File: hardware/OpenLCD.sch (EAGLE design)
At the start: 39 parts, among them Q1 PNP-500mA, Q2 PNP-500mA, Q3 PNP-500mA, U1 ATMEGA328P_TQFP, U2 4BIT-RGB, U3 MIC5205-ADJ, Y2 8MHz

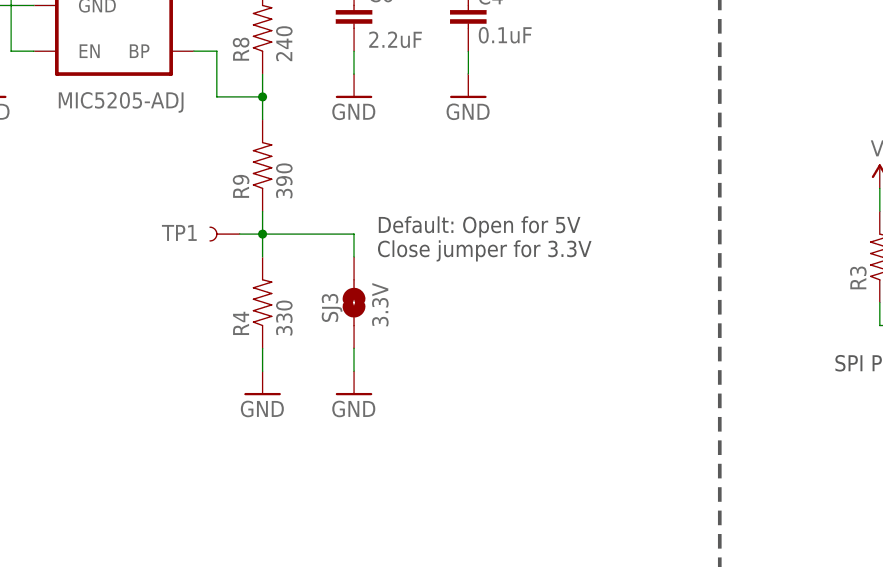
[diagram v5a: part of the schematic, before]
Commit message: Correcting silk
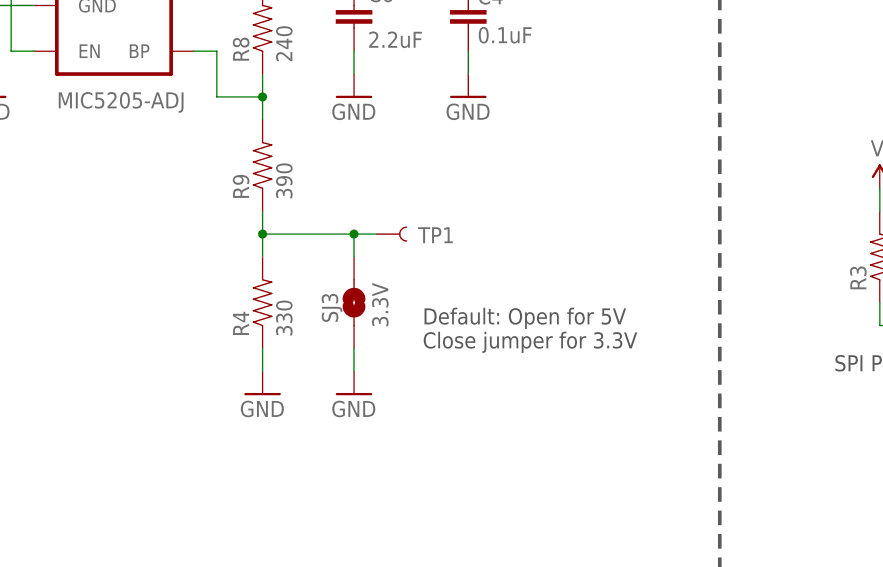
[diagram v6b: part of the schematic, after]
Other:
- moved on the sheet: TP1
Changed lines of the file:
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@@
 <grid distance="0.1" unitdist="inch" unit="inch" style="lines" multiple="1" display="no" altdistance="0.01" altunitdist="inch" altunit="inch"/>
 <layers>
-<layer number="1" name="Top" color="4" fill="1" visible="yes" active="no"/>
-<layer number="2" name="Route2" color="1" fill="3" visible="yes" active="no"/>
-<layer number="3" name="Route3" color="4" fill="3" visible="yes" active="no"/>
-<layer number="4" name="Route4" color="1" fill="4" visible="yes" active="no"/>
-<layer number="5" name="Route5" color="4" fill="4" visible="yes" active="no"/>
-<layer number="6" name="Route6" color="1" fill="8" visible="yes" active="no"/>
-<layer number="7" name="Route7" color="4" fill="8" visible="yes" active="no"/>
-<layer number="8" name="Route8" color="1" fill="2" visible="yes" active="no"/>
-<layer number="9" name="Route9" color="4" fill="2" visible="yes" active="no"/>
-<layer number="10" name="Route10" color="1" fill="7" visible="yes" active="no"/>
-<layer number="11" name="Route11" color="4" fill="7" visible="yes" active="no"/>
-<layer number="12" name="Route12" color="1" fill="5" visible="yes" active="no"/>
-<layer number="13" name="Route13" color="4" fill="5" visible="yes" active="no"/>
-<layer number="14" name="Route14" color="1" fill="6" visible="yes" active="no"/>
-<layer number="15" name="Route15" color="4" fill="6" visible="yes" active="no"/>
-<layer number="16" name="Bottom" color="1" fill="1" visible="yes" active="no"/>
-<layer number="17" name="Pads" color="2" fill="1" visible="yes" active="no"/>
-<layer number="18" name="Vias" color="2" fill="1" visible="yes" active="no"/>
-<layer number="19" name="Unrouted" color="6" fill="1" visible="yes" active="no"/>
-<layer number="20" name="Dimension" color="15" fill="1" visible="yes" active="no"/>
-<layer number="21" name="tPlace" color="16" fill="1" visible="yes" active="no"/>
-<layer number="22" name="bPlace" color="14" fill="1" visible="yes" active="no"/>
-<layer number="23" name="tOrigins" color="15" fill="1" visible="yes" active="no"/>
-<layer number="24" name="bOrigins" color="15" fill="1" visible="yes" active="no"/>
-<layer number="25" name="tNames" color="7" fill="1" visible="yes" active="no"/>
-<layer number="26" name="bNames" color="7" fill="1" visible="yes" active="no"/>
-<layer number="27" name="tValues" color="7" fill="1" visible="yes" active="no"/>
-<layer number="28" name="bValues" color="7" fill="1" visible="yes" active="no"/>
+<layer number="1" name="Top" color="4" fill="1" visible="no" active="no"/>
+<layer number="2" name="Route2" color="1" fill="3" visible="no" active="no"/>
+<layer number="3" name="Route3" color="4" fill="3" visible="no" active="no"/>
+<layer number="4" name="Route4" color="1" fill="4" visible="no" active="no"/>
+<layer number="5" name="Route5" color="4" fill="4" visible="no" active="no"/>
+<layer number="6" name="Route6" color="1" fill="8" visible="no" active="no"/>
+<layer number="7" name="Route7" color="4" fill="8" visible="no" active="no"/>
+<layer number="8" name="Route8" color="1" fill="2" visible="no" active="no"/>
+<layer number="9" name="Route9" color="4" fill="2" visible="no" active="no"/>
+<layer number="10" name="Route10" color="1" fill="7" visible="no" active="no"/>
+<layer number="11" name="Route11" color="4" fill="7" visible="no" active="no"/>
+<layer number="12" name="Route12" color="1" fill="5" visible="no" active="no"/>
+<layer number="13" name="Route13" color="4" fill="5" visible="no" active="no"/>
+<layer number="14" name="Route14" color="1" fill="6" visible="no" active="no"/>
+<layer number="15" name="Route15" color="4" fill="6" visible="no" active="no"/>
+<layer number="16" name="Bottom" color="1" fill="1" visible="no" active="no"/>
+<layer number="17" name="Pads" color="2" fill="1" visible="no" active="no"/>
+<layer number="18" name="Vias" color="2" fill="1" visible="no" active="no"/>
+<layer number="19" name="Unrouted" color="6" fill="1" visible="no" active="no"/>
+<layer number="20" name="Dimension" color="15" fill="1" visible="no" active="no"/>
+<layer number="21" name="tPlace" color="16" fill="1" visible="no" active="no"/>
+<layer number="22" name="bPlace" color="14" fill="1" visible="no" active="no"/>
+<layer number="23" name="tOrigins" color="15" fill="1" visible="no" active="no"/>
+<layer number="24" name="bOrigins" color="15" fill="1" visible="no" active="no"/>
+<layer number="25" name="tNames" color="7" fill="1" visible="no" active="no"/>
+<layer number="26" name="bNames" color="7" fill="1" visible="no" active="no"/>
+<layer number="27" name="tValues" color="7" fill="1" visible="no" active="no"/>
+<layer number="28" name="bValues" color="7" fill="1" visible="no" active="no"/>
 <layer number="29" name="tStop" color="7" fill="3" visible="no" active="no"/>
 <layer number="30" name="bStop" color="7" fill="6" visible="no" active="no"/>
@@
 <layer number="35" name="tGlue" color="7" fill="4" visible="no" active="no"/>
 <layer number="36" name="bGlue" color="7" fill="5" visible="no" active="no"/>
-<layer number="37" name="tTest" color="7" fill="1" visible="yes" active="no"/>
-<layer number="38" name="bTest" color="7" fill="1" visible="yes" active="no"/>
+<layer number="37" name="tTest" color="7" fill="1" visible="no" active="no"/>
+<layer number="38" name="bTest" color="7" fill="1" visible="no" active="no"/>
 <layer number="39" name="tKeepout" color="4" fill="11" visible="no" active="no"/>
 <layer number="40" name="bKeepout" color="1" fill="11" visible="no" active="no"/>
@@
 <layer number="44" name="Drills" color="7" fill="1" visible="no" active="no"/>
 <layer number="45" name="Holes" color="7" fill="1" visible="no" active="no"/>
-<layer number="46" name="Milling" color="3" fill="1" visible="yes" active="no"/>
-<layer number="47" name="Measures" color="7" fill="1" visible="yes" active="no"/>
-<layer number="48" name="Document" color="7" fill="1" visible="yes" active="no"/>
-<layer number="49" name="Reference" color="7" fill="1" visible="yes" active="no"/>
-<layer number="50" name="dxf" color="7" fill="1" visible="yes" active="no"/>
-<layer number="51" name="tDocu" color="6" fill="1" visible="yes" active="no"/>
-<layer number="52" name="bDocu" color="7" fill="1" visible="yes" active="no"/>
-<layer number="53" name="tGND_GNDA" color="7" fill="9" visible="yes" active="no"/>
-<layer number="54" name="bGND_GNDA" color="1" fill="9" visible="yes" active="no"/>
-<layer number="56" name="wert" color="7" fill="1" visible="yes" active="no"/>
-<layer number="57" name="tCAD" color="7" fill="1" visible="yes" active="no"/>
-<layer number="59" name="tCarbon" color="7" fill="1" visible="yes" active="no"/>
-<layer number="60" name="bCarbon" color="7" fill="1" visible="yes" active="no"/>
+<layer number="46" name="Milling" color="3" fill="1" visible="no" active="no"/>
+<layer number="47" name="Measures" color="7" fill="1" visible="no" active="no"/>
+<layer number="48" name="Document" color="7" fill="1" visible="no" active="no"/>
+<layer number="49" name="Reference" color="7" fill="1" visible="no" active="no"/>
+<layer number="50" name="dxf" color="7" fill="1" visible="no" active="no"/>
+<layer number="51" name="tDocu" color="6" fill="1" visible="no" active="no"/>
+<layer number="52" name="bDocu" color="7" fill="1" visible="no" active="no"/>
+<layer number="53" name="tGND_GNDA" color="7" fill="9" visible="no" active="no"/>
+<layer number="54" name="bGND_GNDA" color="1" fill="9" visible="no" active="no"/>
+<layer number="56" name="wert" color="7" fill="1" visible="no" active="no"/>
+<layer number="57" name="tCAD" color="7" fill="1" visible="no" active="no"/>
+<layer number="59" name="tCarbon" color="7" fill="1" visible="no" active="no"/>
+<layer number="60" name="bCarbon" color="7" fill="1" visible="no" active="no"/>
 <layer number="90" name="Modules" color="7" fill="1" visible="yes" active="yes"/>
 <layer number="91" name="Nets" color="2" fill="1" visible="yes" active="yes"/>
@@
 3.3-0.3V = 0.02A * R : R = 150
 3.0V / 235 Ohm = 12.75mA</text>
-<text x="274.32" y="205.74" size="1.778" layer="97">Default: Open for 5V
+<text x="279.4" y="195.58" size="1.778" layer="97">Default: Open for 5V
 Close jumper for 3.3V</text>
 <text x="91.44" y="27.94" size="1.778" layer="97">By default the jumpers support standard
@@
 <instance part="GND9" gate="1" x="76.2" y="30.48"/>
 <instance part="GND10" gate="1" x="76.2" y="5.08"/>
-<instance part="TP1" gate="G$1" x="259.08" y="208.28" smashed="yes" rot="R180">
-<attribute name="NAME" x="250.444" y="207.518" size="1.778" layer="95"/>
-<attribute name="VALUE" x="261.62" y="210.82" size="1.778" layer="96" rot="R180"/>
+<instance part="TP1" gate="G$1" x="274.32" y="208.28" smashed="yes">
+<attribute name="NAME" x="282.956" y="209.042" size="1.778" layer="95" rot="R180"/>
+<attribute name="VALUE" x="271.78" y="205.74" size="1.778" layer="96"/>
 </instance>
 <instance part="TP2" gate="G$1" x="396.24" y="208.28" smashed="yes" rot="R180">
@@
 <wire x1="271.78" y1="208.28" x2="271.78" y2="205.74" width="0.1524" layer="91"/>
 <pinref part="TP1" gate="G$1" pin="1"/>
-<wire x1="259.08" y1="208.28" x2="261.62" y2="208.28" width="0.1524" layer="91"/>
-</segment>
-</net>
+<wire x1="274.32" y1="208.28" x2="271.78" y2="208.28" width="0.1524" layer="91"/>
+<junction x="271.78" y="208.28"/>
+</segment>
+</net>

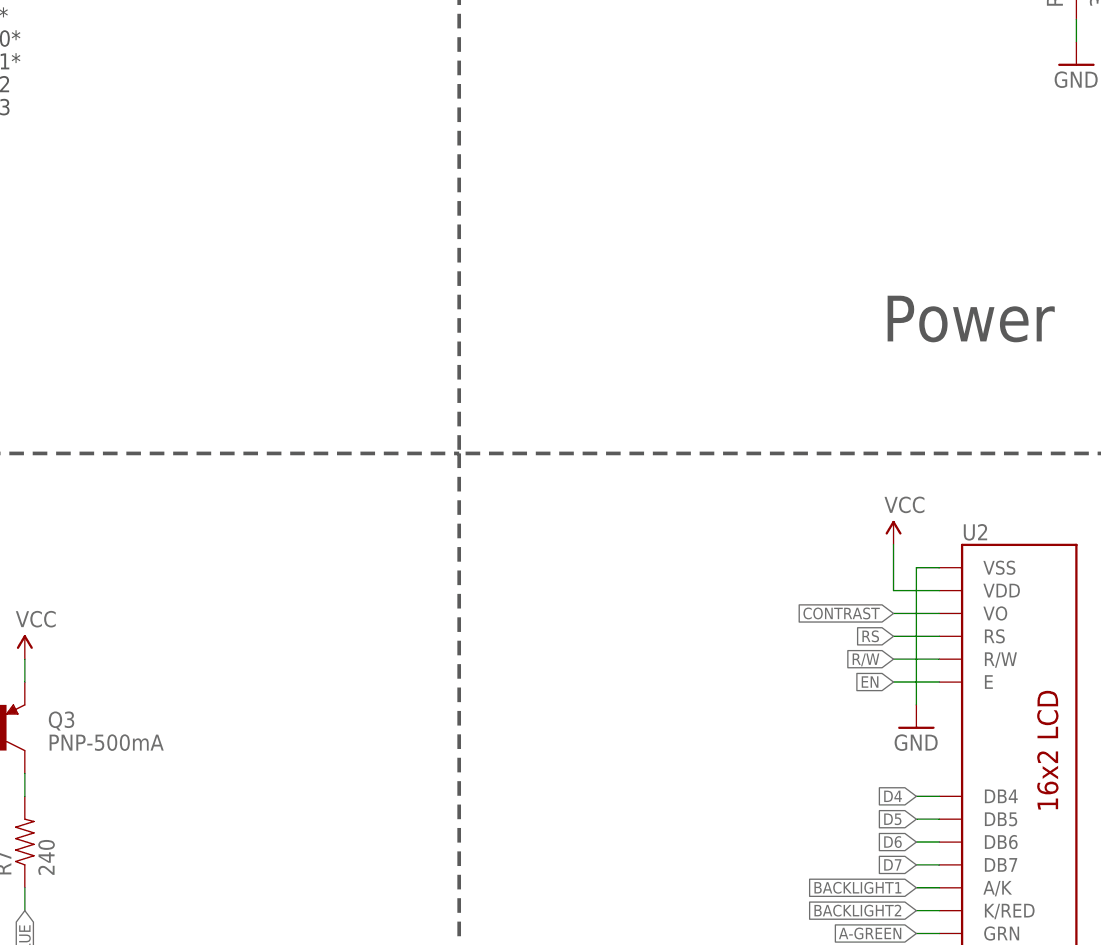
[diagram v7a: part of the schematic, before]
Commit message: Adding Arduino examples. Renaming main firmware.
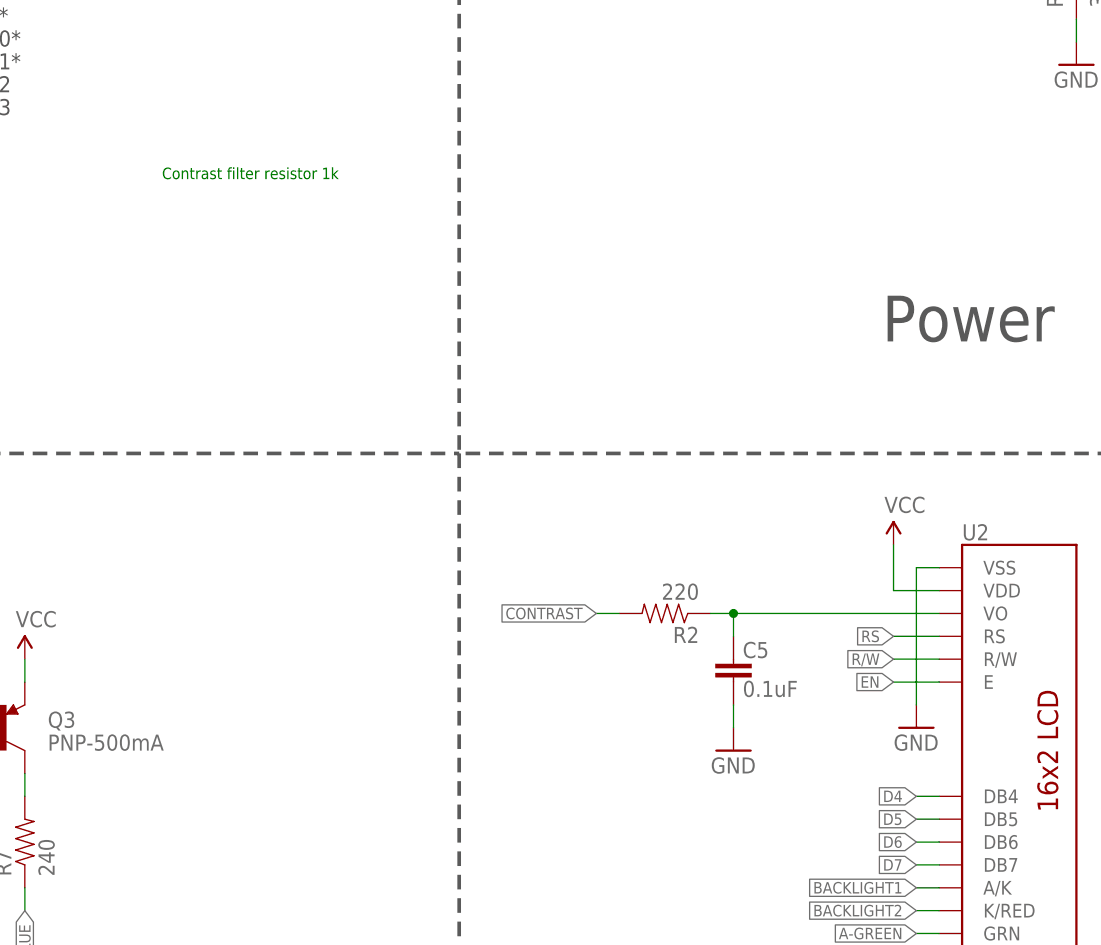
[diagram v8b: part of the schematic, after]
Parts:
- added C5: 0.1uF, SparkFun-Capacitors:0.1UF-25V(+80/-20%)(0603)
- added R2: 220, SparkFun-Resistors:10KOHM-1/10W-1%(0603)0603
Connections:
- new net FILTERED_CONTRAST: C5.2, R2.1, U2.VO
- net CONTRAST: now also R2.2; no longer U2.VO
- net GND: now also C5.1
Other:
- note added: "Contrast filter resistor 1k"
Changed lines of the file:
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@@
 <?xml version="1.0" encoding="utf-8"?>
 <!DOCTYPE eagle SYSTEM "eagle.dtd">
-<eagle version="7.2.0">
+<eagle version="7.1.0">
 <drawing>
 <settings>
@@
 <part name="TP1" library="SparkFun-Passives" deviceset="TEST-POINT" device="3X4" value=""/>
 <part name="TP2" library="SparkFun-Passives" deviceset="TEST-POINT" device="3X4" value=""/>
+<part name="R2" library="SparkFun-Resistors" deviceset="10KOHM-1/10W-1%(0603)" device="0603" value="220"/>
+<part name="C5" library="SparkFun-Capacitors" deviceset="0.1UF-25V(+80/-20%)(0603)" device="" value="0.1uF"/>
+<part name="GND12" library="SparkFun" deviceset="GND" device=""/>
 </parts>
 <sheets>
@@
 operating voltage.</text>
 <text x="198.12" y="251.46" size="1.778" layer="97">In general 5V to 12V is allowed</text>
+<text x="160.02" y="177.8" size="1.27" layer="91">Contrast filter resistor 1k</text>
 </plain>
 <instances>
@@
 <attribute name="VALUE" x="398.78" y="210.82" size="1.778" layer="96" rot="R180"/>
 </instance>
+<instance part="R2" gate="G$1" x="215.9" y="129.54" rot="R180"/>
+<instance part="C5" gate="G$1" x="223.52" y="124.46" smashed="yes" rot="R180">
+<attribute name="NAME" x="224.536" y="124.587" size="1.778" layer="95"/>
+<attribute name="VALUE" x="224.536" y="120.269" size="1.778" layer="96"/>
+</instance>
+<instance part="GND12" gate="1" x="223.52" y="114.3"/>
 </instances>
 <busses>
@@
 <pinref part="JP2" gate="G$1" pin="10"/>
 <wire x1="353.06" y1="129.54" x2="350.52" y2="129.54" width="0.1524" layer="91"/>
+</segment>
+<segment>
+<pinref part="C5" gate="G$1" pin="1"/>
+<pinref part="GND12" gate="1" pin="GND"/>
+<wire x1="223.52" y1="116.84" x2="223.52" y2="119.38" width="0.1524" layer="91"/>
 </segment>
 </net>
@@
 <net name="CONTRAST" class="0">
 <segment>
-<wire x1="246.38" y1="129.54" x2="241.3" y2="129.54" width="0.1524" layer="91"/>
-<label x="241.3" y="129.54" size="1.27" layer="95" rot="MR0" xref="yes"/>
-<pinref part="U2" gate="U1" pin="VO"/>
-</segment>
-<segment>
 <wire x1="114.3" y1="195.58" x2="116.84" y2="195.58" width="0.1524" layer="91"/>
 <label x="116.84" y="195.58" size="1.27" layer="95" xref="yes"/>
 <pinref part="U1" gate="U$1" pin="PB1(OC1A)"/>
+</segment>
+<segment>
+<pinref part="R2" gate="G$1" pin="2"/>
+<wire x1="210.82" y1="129.54" x2="208.28" y2="129.54" width="0.1524" layer="91"/>
+<label x="208.28" y="129.54" size="1.27" layer="95" rot="R180" xref="yes"/>
 </segment>
 </net>
@@
 </segment>
 </net>
+<net name="FILTERED_CONTRAST" class="0">
+<segment>
+<pinref part="U2" gate="U1" pin="VO"/>
+<pinref part="R2" gate="G$1" pin="1"/>
+<wire x1="220.98" y1="129.54" x2="223.52" y2="129.54" width="0.1524" layer="91"/>
+<pinref part="C5" gate="G$1" pin="2"/>
+<wire x1="223.52" y1="129.54" x2="246.38" y2="129.54" width="0.1524" layer="91"/>
+<wire x1="223.52" y1="127" x2="223.52" y2="129.54" width="0.1524" layer="91"/>
+<junction x="223.52" y="129.54"/>
+</segment>
+</net>
